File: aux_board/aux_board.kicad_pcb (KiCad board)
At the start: 4 copper layers, 80 x 80 mm, 113 parts, among them J1 Conn_02x19_Odd_Even, J2 Conn_02x05_Odd_Even, J3 Conn_01x02_Pin, J4 PC104 Conn_02x20_Odd_Even, J5 10155435-00011LF, J6 10155435-00011LF, J7 10155435-00011LF, J8 Conn_01x06, J9 Conn_01x04, SW1 EVP-AA602W, SW2 EVP-AA602W, U1 STM32L496RGT6, U2 TCAN3414, U3 TCAN3414, U4 FT230XS, U5 FT230XS, U6 TPS631000DRLR, U7 TPS631000DRLR, U8 TPS631000DRLR, X1 10MHz

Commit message: inching toward ordering SCI and AUX
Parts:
- added J5: Conn_01x05_Pin, Connector_PinHeader_2.54mm:PinHeader_1x05_P2.54mm_Vertical, F.Cu at (95.4, 62.6)
- added J6: Conn_01x05_Pin, Connector_PinHeader_2.54mm:PinHeader_1x05_P2.54mm_Vertical, F.Cu at (81.3, 62.6)
- moved R2 0.11 mm to (88.8, 68.7)
- moved R1 0.10 mm to (88.5, 96.3)
- moved R29 0.09 mm to (88.8, 67.8)
- moved R28 0.09 mm to (88.5, 95.4)
- moved R3 0.07 mm to (88.7, 81.9)
- moved R30 0.07 mm to (88.7, 80.9)
- moved U7 0.06 mm to (89.3, 70.9)
- moved U8 0.06 mm to (89.0, 84.0)
- renumbered J8 to J10, J9 to J11, J5 to J7, J6 to J8, J7 to J9
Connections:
- U1 pad 51: unconnected-(U1-PC10-Pad51) -> /CAN TO USB/UART4_TX
- U1 pad 52: unconnected-(U1-PC11-Pad52) -> /CAN TO USB/UART4_RX
- U1 pad 53: unconnected-(U1-PC12-Pad53) -> /CAN TO USB/UART5_TX
- U1 pad 54: unconnected-(U1-PD2-Pad54) -> /CAN TO USB/UART5_RX
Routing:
- net /CAN TO USB/UART5_RX: track 0.00 -> 66.9 mm, vias 0 -> 1
- net /CAN TO USB/UART5_TX: track 0.00 -> 65.4 mm, vias 0 -> 1
- net +5V: track 92.5 -> 151.0 mm, vias 3 -> 4
- net /CAN TO USB/UART4_RX: track 0.00 -> 55.8 mm, vias 0 -> 1
- net /CAN TO USB/UART4_TX: track 0.00 -> 55.1 mm, vias 0 -> 1
- net +VBAT: track 35.3 -> 36.2 mm
- net /CAN TO USB/VBUS3: track 47.5 -> 46.9 mm
- net GND: vias 59 -> 72
- added copper zone on F.Cu, net +3V3
- added copper zone on F.Cu, net +5V
- added copper zone on F.Cu, net +VBAT
- added copper zone on F.Cu, net VBUS
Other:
- board text added: "5V"
- board text added: "RX4"
- board text added: "RX5"
- board text added: "TX4"
- board text added: "TX5"

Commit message: tweaking SCI and AUX for production, using common sheets as much as possible
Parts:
- removed the C10 at (90.3, 120.0)
- removed the D6 at (122.5, 66.4)
- removed the R4 at (105.2, 108.7)
- added C35: 100nF, Capacitor_SMD:C_0402_1005Metric_Pad0.74x0.62mm_HandSolder, F.Cu at (91.0, 119.8)
- added R28: 100K, Resistor_SMD:R_0402_1005Metric_Pad0.72x0.64mm_HandSolder, F.Cu at (102.6, 110.7)
- added R30: 100K, Resistor_SMD:R_0402_1005Metric_Pad0.72x0.64mm_HandSolder, F.Cu at (92.0, 119.8)
- moved SW1 19.6 mm to (102.5, 107.6), turned to 90 degrees
- moved SW2 18.9 mm to (87.6, 119.3), turned to 0 degrees
- moved D1 3.74 mm to (122.6, 66.2)
- moved D2 3.74 mm to (122.6, 73.3)
- moved D3 3.74 mm to (122.6, 69.8)
- renumbered C11 to C10, C12 to C11, C13 to C12, C14 to C13, C15 to C14, C16 to C15, C17 to C16, C18 to C17, C19 to C18, C20 to C19, C21 to C20, C22 to C21, C23 to C22, C24 to C23, C25 to C24, C26 to C25, C27 to C26, C28 to C27, C29 to C28, C30 to C29, C31 to C30, C32 to C31, C33 to C32, C34 to C33, C35 to C34, D3 to D1, D11 to D10, D12 to D11, D13 to D12, D14 to D13, D15 to D14, D16 to D15, D17 to D16, D4 to D2, D5 to D3, D1 to D4, D2 to D5, D7 to D6, D8 to D7, D9 to D8, D10 to D9, J3 to J2, J2 to J3, R11 to R10, R12 to R11, R13 to R12, R14 to R13, R15 to R14, R16 to R15, R17 to R16, R18 to R17, R19 to R18, R20 to R19, R21 to R20, R22 to R21, R23 to R22, R24 to R23, R25 to R24, R26 to R25, R27 to R26, R28 to R27, R30 to R31, R5 to R4, R6 to R5, R7 to R6, R8 to R7, R9 to R8, R10 to R9
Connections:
- D4 pad 1: VCC -> VBUS
- SW1 pad 1: unconnected-(SW1-Pad1) -> +3V3
- SW1 pad 2: unconnected-(SW1-Pad2) -> /CAN TO USB/BOOT
- SW1 pad 3: /CAN TO USB/NRST -> unconnected-(SW1-Pad3)
- SW1 pad 4: GND -> unconnected-(SW1-Pad4)
- SW2 pad 3: +3V3 -> /CAN TO USB/NRST
- SW2 pad 4: /CAN TO USB/BOOT -> GND
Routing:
- net /CAN TO USB/VBUS1: track 65.7 -> 69.6 mm
- net /CAN TO USB/VBUS2: track 21.0 -> 24.7 mm
- net /CAN TO USB/VBUS3: track 46.9 -> 50.7 mm
- net VCC: track 3.70 -> 0.00 mm
- net VBUS: track 81.2 -> 84.3 mm
- net /CAN TO USB/BOOT: track 44.7 -> 43.8 mm
- net +3V3: track 42.1 -> 42.6 mm, vias 12 -> 13
- net GND: track 9.47 -> 9.65 mm, vias 72 -> 75
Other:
- board text added: "RESET"

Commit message: clenup BOM for SCI and AUX
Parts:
- removed the R22 at (116.0, 127.4)
- added C18: 10uF, Capacitor_SMD:C_0603_1608Metric_Pad1.08x0.95mm_HandSolder, F.Cu at (126.2, 102.7)
- added C24: 10uF, Capacitor_SMD:C_0603_1608Metric_Pad1.08x0.95mm_HandSolder, F.Cu at (126.9, 82.6)
- added FB1: 120R, Inductor_SMD:L_0603_1608Metric_Pad1.05x0.95mm_HandSolder, F.Cu at (124.7, 102.7)
- added FB2: 120R, Inductor_SMD:L_0603_1608Metric_Pad1.05x0.95mm_HandSolder, F.Cu at (125.4, 82.6)
- added R1: 330K, Resistor_SMD:R_0402_1005Metric_Pad0.72x0.64mm_HandSolder, F.Cu at (96.6, 114.8)
- added R27: 1K, Resistor_SMD:R_0402_1005Metric_Pad0.72x0.64mm_HandSolder, F.Cu at (116.2, 121.0)
- C22: renamed from C21; value 47p -> 47pF
- C23: renamed from C22; value 47p -> 47pF
- C28: renamed from C26; value 47p -> 47pF
- C29: renamed from C27; value 47p -> 47pF
- R13: renamed from R12; footprint Resistor_SMD:R_0603_1608Metric_Pad0.98x0.95mm_HandSolder -> Resistor_SMD:R_0402_1005Metric_Pad0.72x0.64mm_HandSolder
- R14: renamed from R13; footprint Resistor_SMD:R_0603_1608Metric_Pad0.98x0.95mm_HandSolder -> Resistor_SMD:R_0402_1005Metric_Pad0.72x0.64mm_HandSolder
- R19: renamed from R18; footprint Resistor_SMD:R_0603_1608Metric_Pad0.98x0.95mm_HandSolder -> Resistor_SMD:R_0402_1005Metric_Pad0.72x0.64mm_HandSolder
- R20: renamed from R19; footprint Resistor_SMD:R_0603_1608Metric_Pad0.98x0.95mm_HandSolder -> Resistor_SMD:R_0402_1005Metric_Pad0.72x0.64mm_HandSolder
- R21: renamed from R20; footprint Resistor_SMD:R_0603_1608Metric_Pad0.98x0.95mm_HandSolder -> Resistor_SMD:R_0402_1005Metric_Pad0.72x0.64mm_HandSolder
- R22: renamed from R21; footprint Resistor_SMD:R_0603_1608Metric_Pad0.98x0.95mm_HandSolder -> Resistor_SMD:R_0402_1005Metric_Pad0.72x0.64mm_HandSolder
- R3: renamed from R2; value 673K -> 665K
- moved R23 1.69 mm to (116.2, 127.5), turned to 0 degrees
- moved R24 1.68 mm to (116.2, 125.9), turned to 0 degrees
- moved R25 1.66 mm to (116.2, 124.3), turned to 0 degrees
- moved R26 1.65 mm to (116.2, 122.6), turned to 0 degrees
- moved C4 0.81 mm to (97.6, 115.4), turned to 90 degrees
- moved R13 0.56 mm to (133.5, 114.5)
- moved R22 0.54 mm to (133.6, 118.8)
- moved R21 0.52 mm to (133.6, 130.2)
- moved R19 0.51 mm to (133.4, 94.5)
- moved R20 0.46 mm to (133.4, 83.2)
- moved R14 0.45 mm to (133.5, 103.1)
- moved C26 0.22 mm to (123.9, 82.6)
- renumbered C18 to C21, C24 to C25, C25 to C26, C23 to C27, C28 to C30, C29 to C31, C30 to C32, C31 to C33, C32 to C34, C33 to C35, C34 to C36, C35 to C37, C36 to C38, C37 to C39, C38 to C40, R9 to R10, R10 to R11, R11 to R12, R14 to R15, R15 to R16, R16 to R17, R17 to R18, R1 to R2, R27 to R28, R28 to R29, R29 to R30, R30 to R31, R31 to R32, R3 to R4, R4 to R5, R5 to R6, R6 to R7, R7 to R8, R8 to R9
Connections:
- net Net-(U4-CBUS1) renamed /CAN TO USB/FTDI/TXLED
- net Net-(U4-CBUS2) renamed /CAN TO USB/FTDI/RXLED
- net Net-(U5-CBUS1) renamed /CAN TO USB/FTDI1/TXLED
- net Net-(U5-CBUS2) renamed /CAN TO USB/FTDI1/RXLED
- C19 pad 1: +5V -> Net-(U4-VCC)
- C20 pad 1: +5V -> Net-(U4-VCC)
- C25 pad 1: +5V -> Net-(U5-VCC)
- C26 pad 1: +5V -> Net-(U5-VCC)
- R23 pad 1: Net-(D13-A) -> /CAN TO USB/LED1
- R23 pad 2: /CAN TO USB/LED2 -> Net-(D12-A)
- R24 pad 1: Net-(D14-A) -> /CAN TO USB/LED2
- R24 pad 2: /CAN TO USB/LED3 -> Net-(D13-A)
- R25 pad 1: Net-(D15-A) -> /CAN TO USB/LED3
- R25 pad 2: /CAN TO USB/LED4 -> Net-(D14-A)
- R26 pad 1: Net-(D16-A) -> /CAN TO USB/LED4
- R26 pad 2: /CAN TO USB/LED5 -> Net-(D15-A)
- U4 pad 12: +5V -> Net-(U4-VCC)
- U5 pad 12: +5V -> Net-(U5-VCC)
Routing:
- net +5V: track 151.0 -> 76.6 mm, vias 4 -> 1
- net /CAN TO USB/VBUS3: track 50.7 -> 59.6 mm, vias 3 -> 4
- net /CAN TO USB/VBUS2: track 24.7 -> 30.5 mm, vias 3 -> 4
- net Net-(U4-VCC): track 0.00 -> 5.05 mm
- net Net-(U5-VCC): track 0.00 -> 4.70 mm
- net VBUS: track 84.3 -> 82.9 mm
- net /CAN TO USB/FTDI/TXLED: track 17.8 -> 19.1 mm
- net /CAN TO USB/FTDI1/TXLED: track 16.8 -> 18.1 mm
- net /CAN TO USB/FTDI1/3V3: track 29.4 -> 30.5 mm
- net /CAN TO USB/NRST: track 43.5 -> 42.7 mm
- net GND: track 9.65 -> 10.2 mm, vias 75 -> 79

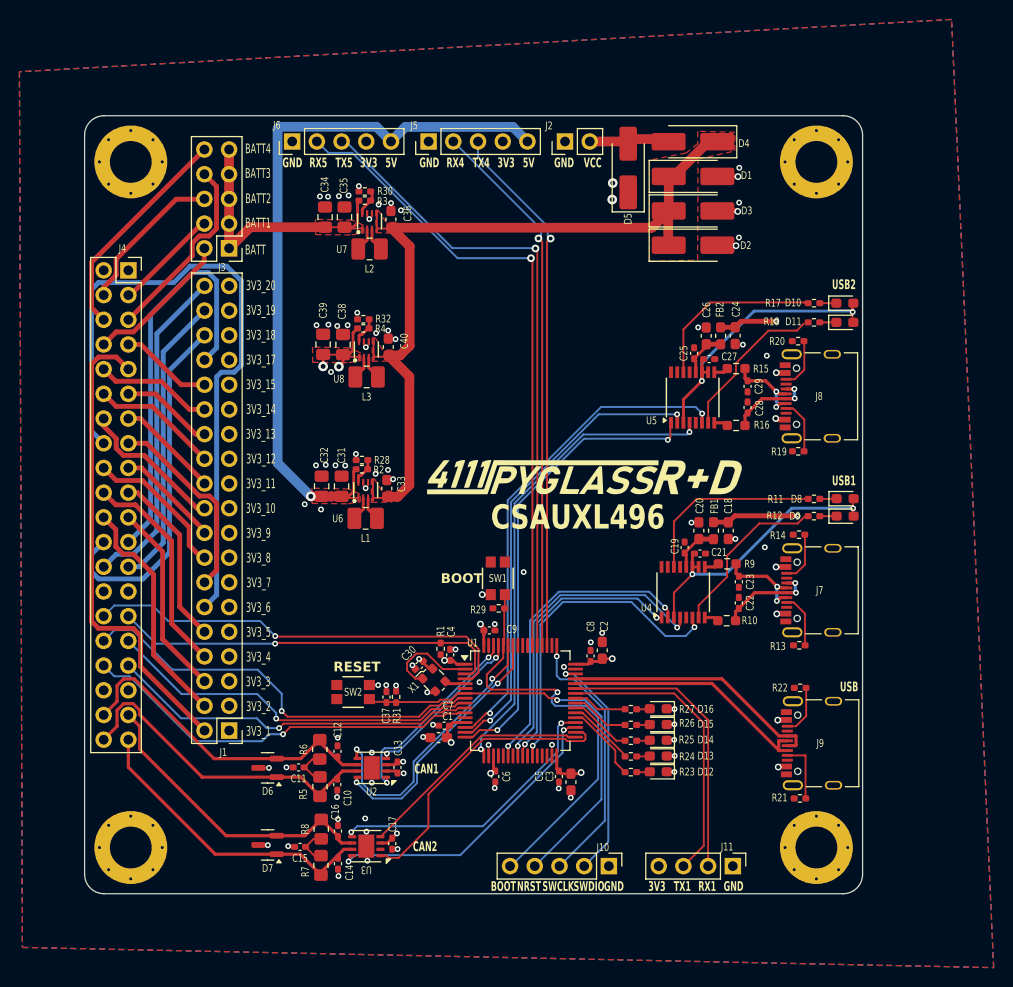
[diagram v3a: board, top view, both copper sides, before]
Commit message: QC, add second 3V regulator to AUX, INT pullups on AUX SCI AVI
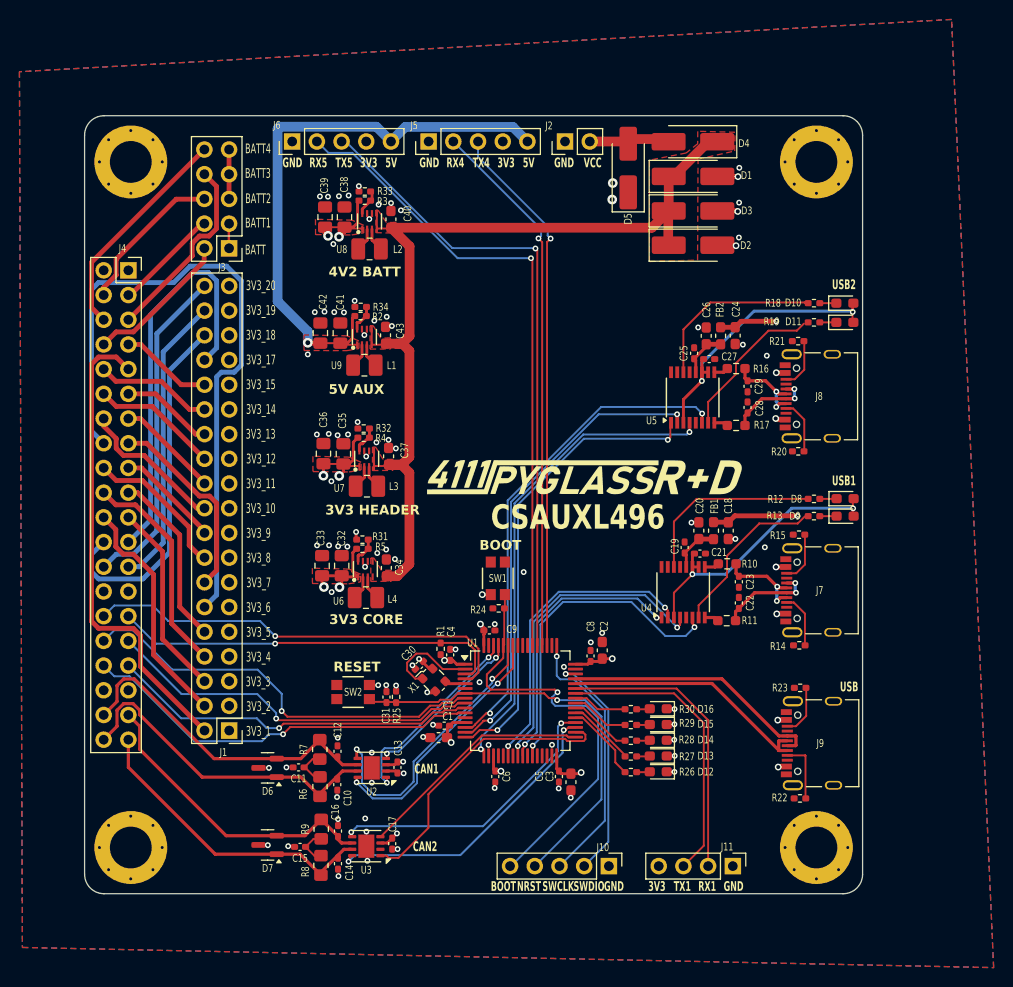
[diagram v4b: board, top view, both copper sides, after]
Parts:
- added C32: 47uF, Capacitor_SMD:C_0805_2012Metric_Pad1.18x1.45mm_HandSolder, F.Cu at (86.4, 106.3)
- added C33: 47uF, Capacitor_SMD:C_0805_2012Metric_Pad1.18x1.45mm_HandSolder, F.Cu at (84.4, 106.3)
- added C34: 22uF, Capacitor_SMD:C_0603_1608Metric_Pad1.08x0.95mm_HandSolder, F.Cu at (91.0, 106.5)
- added L4: 1uH, Inductor_SMD:L_1008_2520Metric_Pad1.43x2.20mm_HandSolder, F.Cu at (88.9, 109.5)
- added R31: 91K, Resistor_SMD:R_0402_1005Metric_Pad0.72x0.64mm_HandSolder, F.Cu at (88.6, 103.6)
- added R5: 511K, Resistor_SMD:R_0402_1005Metric_Pad0.72x0.64mm_HandSolder, F.Cu at (88.6, 104.5)
- added U6: TPS631000DRLR, Common:TPS631000DRLR_TEX, F.Cu at (88.9, 106.6)
- SW1, SW2: footprint Project:EVP602AA -> Common:EVP602AA
- moved C41 15.8 mm to (86.3, 82.3)
- moved C42 15.8 mm to (84.2, 82.3)
- moved C43 15.8 mm to (90.9, 82.6)
- moved L1 15.8 mm to (88.8, 85.6)
- moved R2 15.8 mm to (88.4, 80.6)
- moved R34 15.8 mm to (88.4, 79.7)
- moved U9 15.8 mm to (88.8, 82.7)
- moved C35 11.2 mm to (86.6, 94.8)
- moved C36 11.2 mm to (84.6, 94.7)
- moved C37 11.2 mm to (91.3, 95.0)
- moved L3 11.2 mm to (89.0, 98.1)
- moved R32 11.2 mm to (88.7, 92.2)
- moved R4 11.2 mm to (88.7, 93.1)
- moved U7 11.2 mm to (89.0, 95.3)
- moved C38 2.00 mm to (86.7, 70.4)
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- renumbered C37 to C31, C38 to C35, C39 to C36, C40 to C37, C34 to C38, C35 to C39, C36 to C40, C31 to C41, C32 to C42, C33 to C43, R9 to R10, R10 to R11, R11 to R12, R12 to R13, R13 to R14, R14 to R15, R15 to R16, R16 to R17, R17 to R18, R18 to R19, R19 to R20, R20 to R21, R21 to R22, R22 to R23, R29 to R24, R31 to R25, R23 to R26, R24 to R27, R25 to R28, R26 to R29, R27 to R30, R30 to R33, R28 to R34, R5 to R6, R6 to R7, R7 to R8, R8 to R9, U8 to U7, U7 to U8, U6 to U9
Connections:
- C1 pad 1: +3V3 -> +3V3_Core
- C13 pad 1: +3V3 -> +3V3_Core
- C17 pad 1: +3V3 -> +3V3_Core
- C2 pad 1: +3V3 -> +3V3_Core
- C3 pad 1: +3V3 -> +3V3_Core
- C30 pad 1: +3V3 -> +3V3_Core
- C4 pad 1: +3V3 -> +3V3_Core
- C5 pad 1: +3V3 -> +3V3_Core
- C6 pad 1: +3V3 -> +3V3_Core
- C7 pad 1: +3V3 -> +3V3_Core
- C8 pad 1: +3V3 -> +3V3_Core
- C9 pad 1: +3V3 -> +3V3_Core
- J11 pad 4: +3V3 -> +3V3_Core
- J5 pad 4: +3V3 -> +3V3_Core
- J6 pad 4: +3V3 -> +3V3_Core
- R1 pad 1: +3V3 -> +3V3_Core
- R25 pad 1: +3V3 -> +3V3_Core
- SW1 pad 1: +3V3 -> +3V3_Core
- U1 pad 1: +3V3 -> +3V3_Core
- U1 pad 13: +3V3 -> +3V3_Core
- U1 pad 19: +3V3 -> +3V3_Core
- U1 pad 32: +3V3 -> +3V3_Core
- U1 pad 48: +3V3 -> +3V3_Core
- U1 pad 64: +3V3 -> +3V3_Core
- U2 pad 3: +3V3 -> +3V3_Core
- U3 pad 3: +3V3 -> +3V3_Core
- X1 pad 4: +3V3 -> +3V3_Core
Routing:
- net +3V3_Core: track 0.00 -> 42.7 mm, vias 0 -> 13
- net +3V3: track 43.0 -> 9.78 mm, vias 13 -> 2
- net +VBAT: track 36.0 -> 17.2 mm, vias 0 -> 2
- net +5V: track 76.6 -> 59.7 mm
- net VBUS: track 82.9 -> 94.8 mm
- net /Regulator 3V4/R-: track 0.00 -> 2.86 mm
- net /Regulator 3V4/LX1: track 0.00 -> 2.53 mm
- net /Regulator 3V4/LX2: track 0.00 -> 2.48 mm
- net GND: track 10.2 -> 11.0 mm, vias 79 -> 89
- added copper zone on F.Cu, net +3V3_Core
- added copper zone on In2.Cu, net +3V3_Core
- added copper zone on In2.Cu, net +VBAT
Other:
- board text added: "3V3 CORE"
- board text added: "3V3 HEADER"
- board text added: "4V2 BATT"
- board text added: "5V AUX"
